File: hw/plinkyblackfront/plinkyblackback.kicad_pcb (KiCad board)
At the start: 2 copper layers, 121.9 x 128.3 mm, 6 parts, among them M1 MountingHole_3.2mm_M3, M2 MountingHole_3.2mm_M3, M3 MountingHole_3.2mm_M3, M4 MountingHole_3.2mm_M3

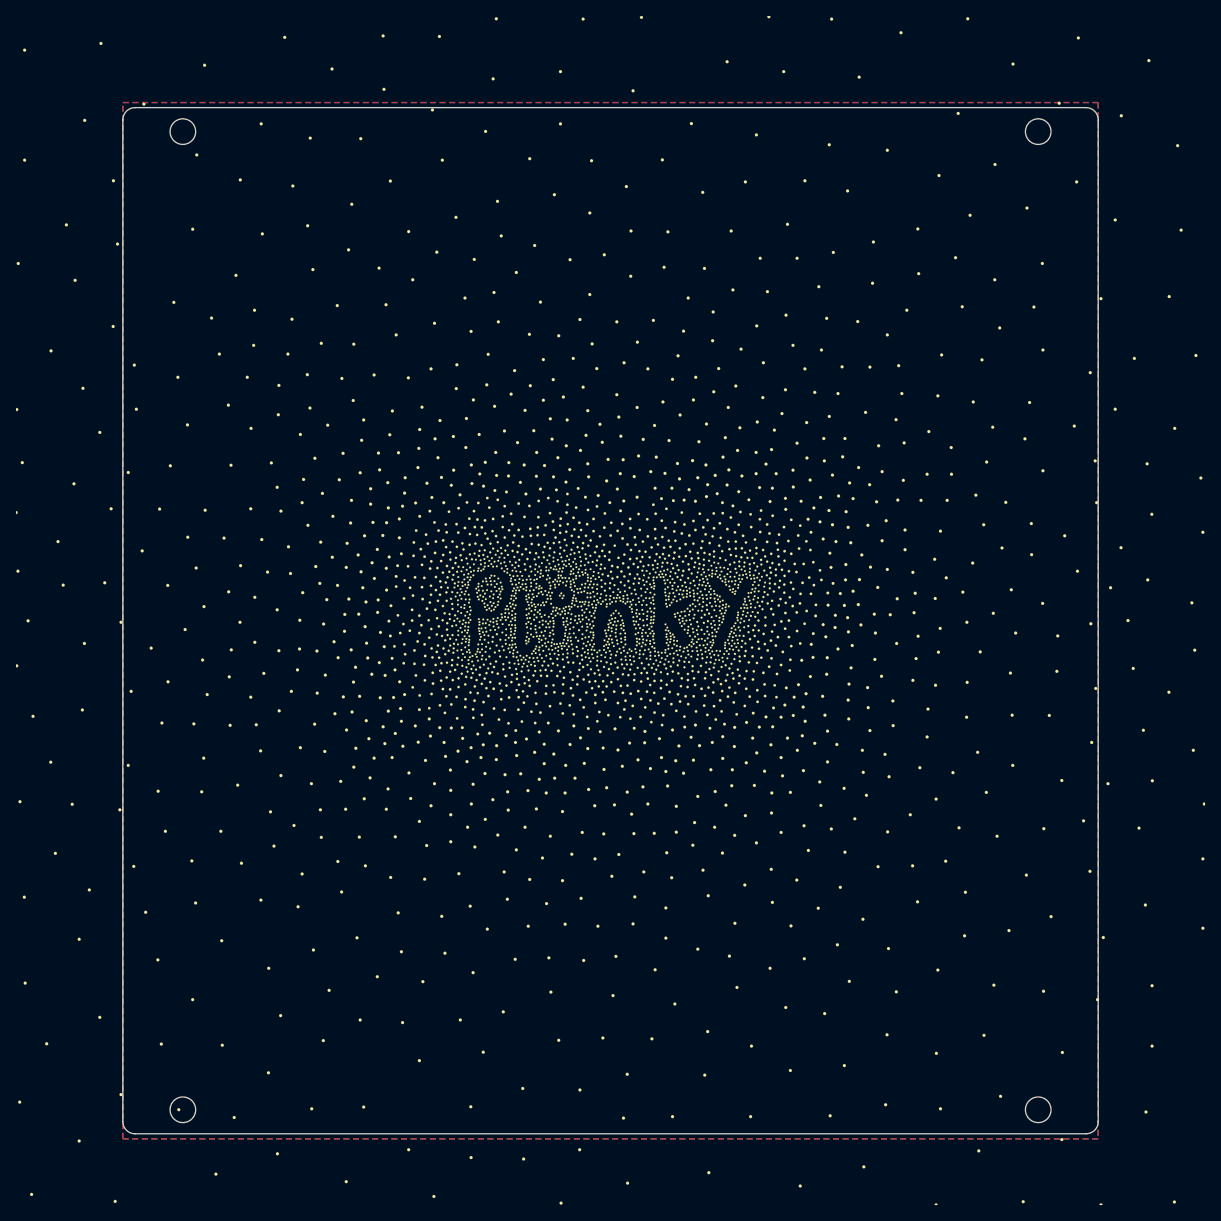
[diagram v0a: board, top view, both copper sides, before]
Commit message: production adjustments and convert testjig to kicad7
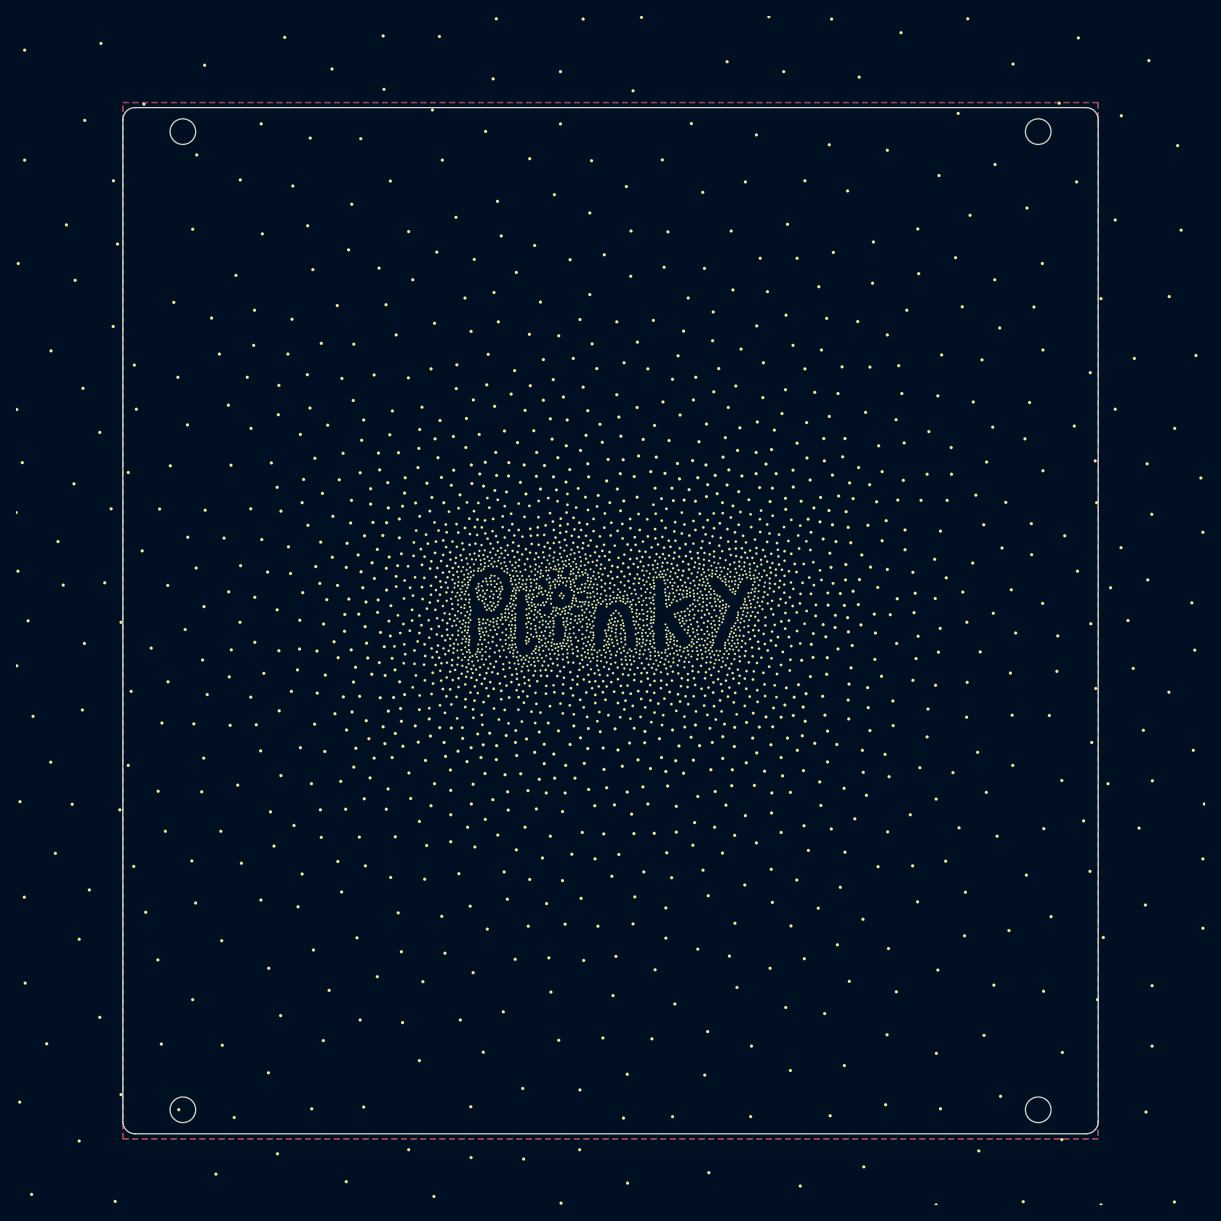
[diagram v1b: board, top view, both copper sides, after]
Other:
- net class Default removed
- board text added: "JLCJLCJLCJLC"
